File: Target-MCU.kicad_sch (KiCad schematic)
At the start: 25 parts, among them Q3 DMG1012UW-7, SW4 SKRPASE010

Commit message: Update schematic
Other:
- note added: "All the Target MCU pins are outputs from this sheet."
- note added: "RST_OUT is the output RST pin from the flash/debug probe (so it's the input RST pin for the Target MCU). With this switch, you can trigger a RST manually."
- note added: "Reset"
- note added: "SWDIO_OUT and RST_OUT are the output SWDIO and RST signals from the flash/debug probe. They flash new firmware to the Target MCU. TX and RX also come from the flash/debug probe. They set up a UART communication channel with the Target MCU."
- note added: "Sheet Output"
- note added: "Sheet input"
- moved on the sheet: C26, C27, C28, C29, C30, C32, C33, C34, C35, C36, C37, C38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

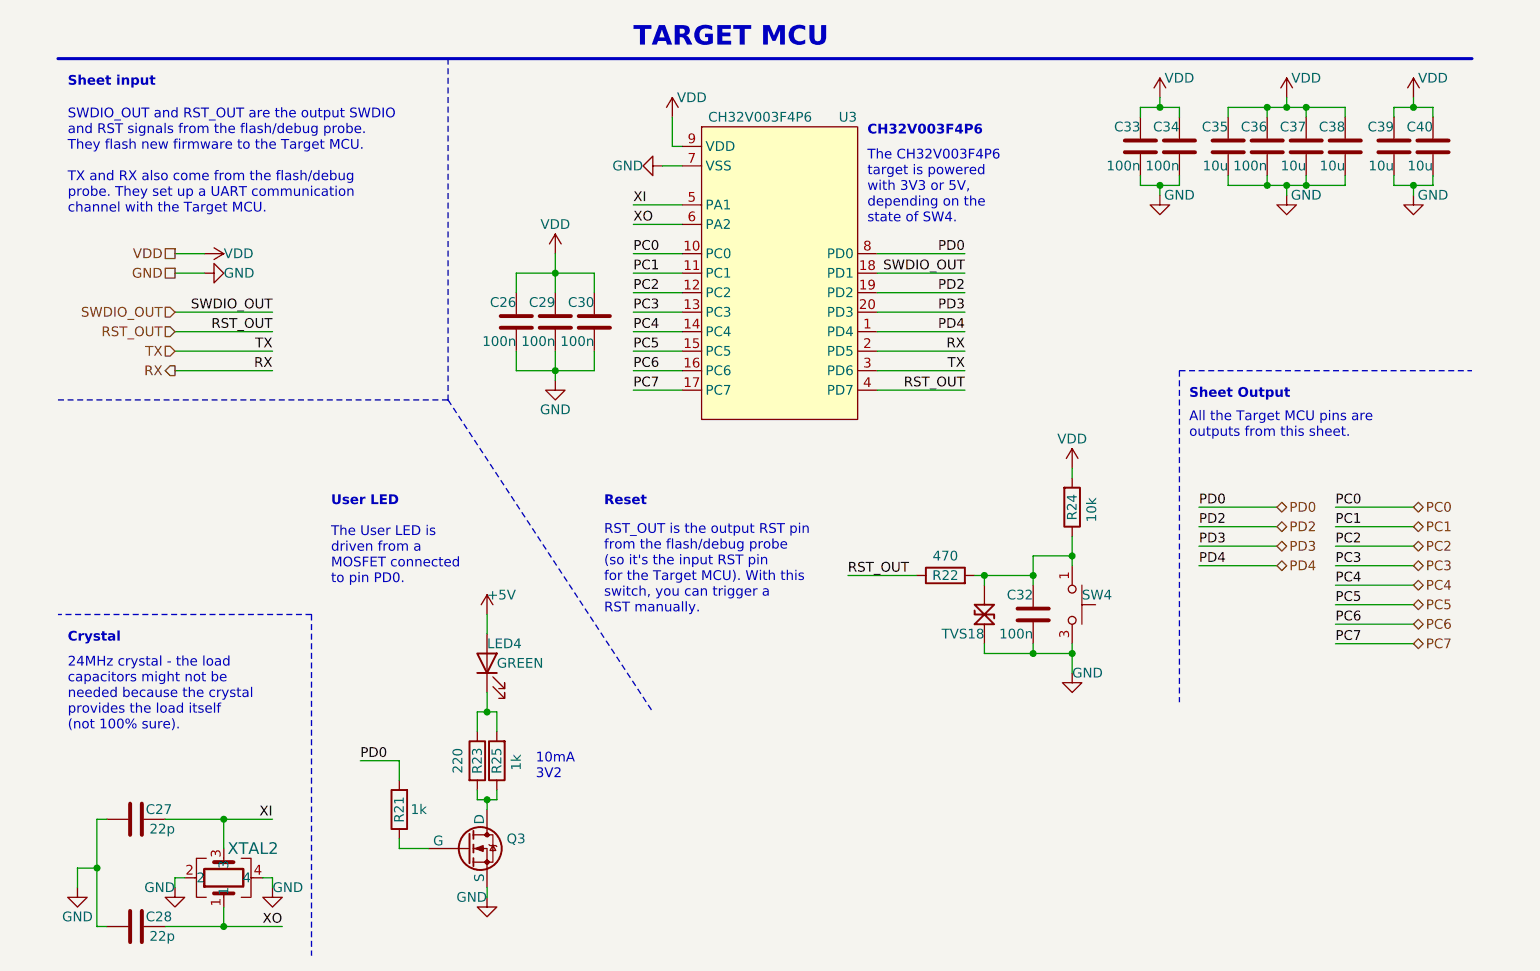
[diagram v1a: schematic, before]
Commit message: Renumber designators and draw new silkscreen
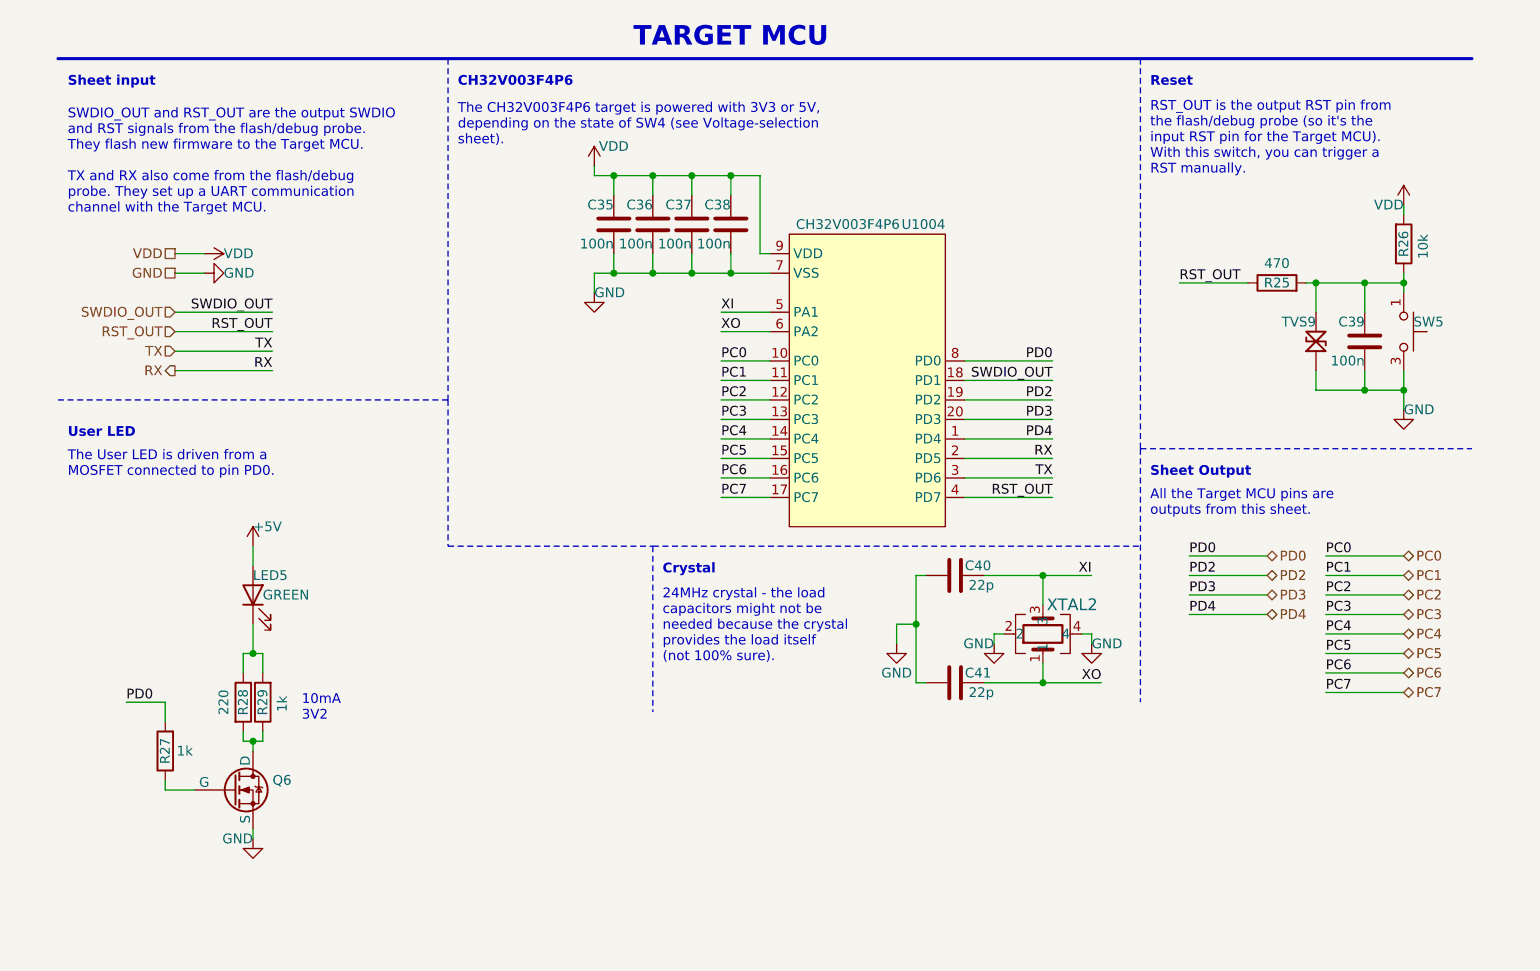
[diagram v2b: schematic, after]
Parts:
- removed C33, C34: 100n, Capacitor_SMD:C_0402_1005Metric_Pad0.74x0.62mm_HandSolder, symbol Device:C
- removed C35, C37, C38, C39, C40: 10u, Capacitor_SMD:C_0805_2012Metric, symbol Device:C
- renumbered C36 to C35, C26 to C36, C29 to C37, C30 to C38, C32 to C39, C27 to C40, C28 to C41, LED4 to LED5, Q3 to Q6, R22 to R25, R24 to R26, R21 to R27, R23 to R28, R25 to R29, SW4 to SW5, TVS18 to TVS9, U3 to U1004
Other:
- note added: "The CH32V003F4P6 target is powered with 3V3 or 5V, depending on the state of SW4 (see Voltage-selection sheet)."
- note removed: "The CH32V003F4P6 target is powered with 3V3 or 5V, depending on the state of SW4."
- moved on the sheet: C35, C36, C37, C38, C39, C40, C41, LED5, Q6, R25, R26, R27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

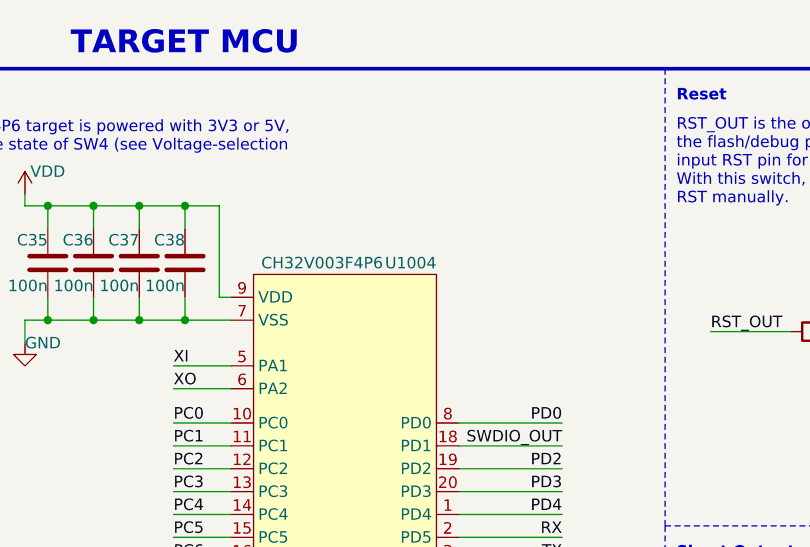
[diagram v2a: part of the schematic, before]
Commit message: Change J3 and J4 part numbers
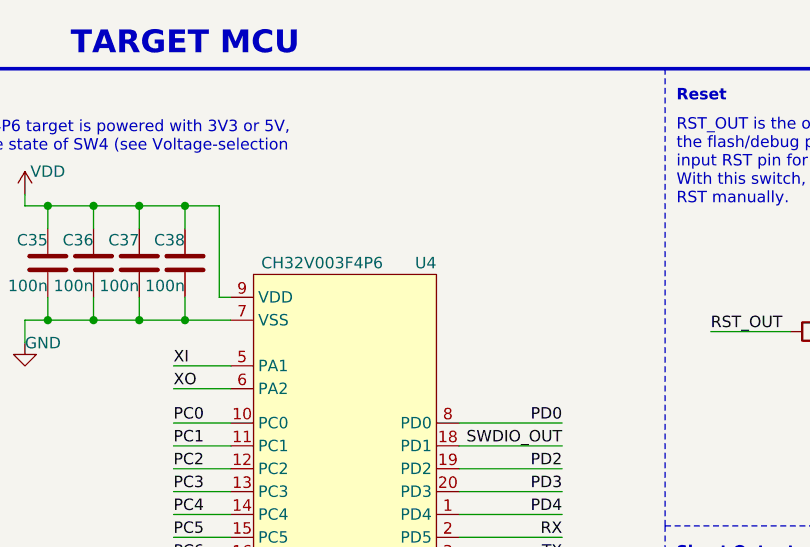
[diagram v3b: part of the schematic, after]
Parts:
- renumbered U1004 to U4
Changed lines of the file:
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@@
   (symbol (lib_id "Tiny_Scarab:CH32V003F4P6") (at 118.11 57.15 0) (unit 1)
     (in_bom yes) (on_board yes) (dnp no)
-    (property "Reference" "U1004" (at 128.27 40.64 0)
+    (property "Reference" "U4" (at 128.27 40.64 0)
       (effects (font (size 1.27 1.27)) (justify right))
     )
@@
       (project "tiny-scarab"
         (path "/156c5422-ee07-49a4-8263-a2dbd26b90bd/d0c4b0c3-1e7e-4a4c-add3-8d4a3a10843d"
-          (reference "U1004") (unit 1)
+          (reference "U4") (unit 1)
         )
       )

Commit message: Replace TVS diodes with cheaper alternative
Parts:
- TVS9: SPN CDSOD323-T05LCTR-ND -> (none); Supplier DigiKey -> (none)
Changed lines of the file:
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@@
       (effects (font (size 1.27 1.27)) (justify left bottom) hide)
-    )
-    (property "Supplier" "DigiKey" (at 186.69 60.96 0)
-      (effects (font (size 1.27 1.27)) (justify left) hide)
-    )
-    (property "SPN" "CDSOD323-T05LCTR-ND" (at 186.69 63.5 0)
-      (effects (font (size 1.27 1.27)) (justify left) hide)
     )
     (property "JLCPCB Part #" "C840637" (at 176.53 55.88 0)

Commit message: Clean up symbols library
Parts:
- LED5: DigiKey (none) -> 846-CSL0902ET1TR-ND
- Q6: DigiKey (none) -> DMG1012UW-7DITR-ND; Farnell (none) -> 3127309; Mouser (none) -> 621-DMG1012UW-7
- SW5: DigiKey (none) -> 4809-SKRPADE010TR-ND; Farnell (none) -> 3261826; Mouser (none) -> 688-SKRPASE010
- TVS9: Farnell (none) -> 1824861; Mouser (none) -> 652-CDSOD323-T05LC
- U4: AliExpress (none) -> 1005005036714708
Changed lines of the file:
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@@
       (effects (font (size 1.27 1.27)) (justify left) hide)
     )
+    (property "Farnell" "1824861" (at 176.53 41.91 0)
+      (effects (font (size 1.27 1.27)) hide)
+    )
+    (property "Mouser" "652-CDSOD323-T05LC" (at 176.53 44.45 0)
+      (effects (font (size 1.27 1.27)) hide)
+    )
     (pin "2")
     (pin "1")
@@
       (effects (font (size 1.27 1.27)) hide)
     )
-    (property "Datasheet" "" (at 212.09 54.61 0)
+    (property "Datasheet" "https://www.farnell.com/datasheets/2864500.pdf" (at 212.09 54.61 0)
       (effects (font (size 1.27 1.27)) hide)
     )
@@
     )
     (property "JLCPCB Part #" "C470427" (at 199.39 54.61 0)
+      (effects (font (size 1.27 1.27)) hide)
+    )
+    (property "DigiKey" "4809-SKRPADE010TR-ND" (at 200.66 54.61 0)
+      (effects (font (size 1.27 1.27)) hide)
+    )
+    (property "Farnell" "3261826" (at 198.12 54.61 0)
+      (effects (font (size 1.27 1.27)) hide)
+    )
+    (property "Mouser" "688-SKRPASE010" (at 195.58 54.61 0)
       (effects (font (size 1.27 1.27)) hide)
     )
@@
     (property "JLCPCB Part #" "C5187096" (at 118.11 57.15 0)
       (effects (font (size 1.27 1.27)) hide)
+    )
+    (property "AliExpress" "1005005036714708" (at 118.11 33.02 0)
+      (effects (font (size 1.27 1.27)) hide)
+    )
+    (property "DigiKey" "" (at 118.11 57.15 0)
+      (effects (font (size 1.27 1.27)))
+    )
+    (property "Farnell" "" (at 118.11 57.15 0)
+      (effects (font (size 1.27 1.27)))
+    )
+    (property "Mouser" "" (at 118.11 57.15 0)
+      (effects (font (size 1.27 1.27)))
     )
     (pin "17")
@@
       (effects (font (size 1.27 1.27)) hide)
     )
+    (property "DigiKey" "" (at 140.97 93.98 0)
+      (effects (font (size 1.27 1.27)) hide)
+    )
+    (property "Farnell" "" (at 140.97 93.98 0)
+      (effects (font (size 1.27 1.27)) hide)
+    )
+    (property "Mouser" "" (at 140.97 93.98 0)
+      (effects (font (size 1.27 1.27)) hide)
+    )
     (pin "3")
     (pin "4")
@@
       (effects (font (size 1.27 1.27)) hide)
     )
+    (property "DigiKey" "846-CSL0902ET1TR-ND" (at 25.4 88.9 0)
+      (effects (font (size 1.27 1.27)) hide)
+    )
     (pin "2")
     (pin "1")
@@
       (effects (font (size 1.27 1.27)) hide)
     )
+    (property "DigiKey" "DMG1012UW-7DITR-ND" (at 35.56 97.79 0)
+      (effects (font (size 1.27 1.27)) hide)
+    )
+    (property "Farnell" "3127309" (at 35.56 100.33 0)
+      (effects (font (size 1.27 1.27)) hide)
+    )
+    (property "Mouser" "621-DMG1012UW-7" (at 35.56 102.87 0)
+      (effects (font (size 1.27 1.27)) hide)
+    )
